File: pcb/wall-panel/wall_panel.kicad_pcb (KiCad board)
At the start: 6 copper layers, 75 x 79 mm, 121 parts, among them J1 USB_C_Receptacle_USB2.0_14P, J10 THD-20-R, J15 THD-20-R, J16 Micro_SD_Card_Det, J17 USB_C_Receptacle_USB2.0_14P, J18 THD-20-R, J2 USB_C_Receptacle_USB2.0_14P, J4 Conn_01x02_Socket, J5 F31L-1A7H1-11030, J6 690-019-298-412, SW1 power reset, SW2 cpu reset, U1 FSUSB42MUX, U10 RT9742GGJ5, U11 MT3608, U2 USB2514B-I/M2, U3 TPD4EUSB30, U4 AP22653W6, U5 DS3231M, U6 RT9742SNGV, U7 LP5907MFX-2.8, U9 74LVC1G07SE-7, Y1 ABM8G-24.000MHZ-18-D2Y-T

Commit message: wall panel v0.3
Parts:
- removed kibuzzard-68AB3EB0: G***, kibuzzard-68AB3EB0
- removed kibuzzard-6960BEF1: G***, kibuzzard-6960BEF1
- added kibuzzard-6981E919: G***, kibuzzard-6981E919, B.Cu at (69.8, 131.0)
- added kibuzzard-6984C46F: G***, kibuzzard-6984C46F, B.Cu at (111.5, 129.2)
- J5: value F31L-1A7H1-11030 -> SFV30R-4STBE1HLF; footprint F31L-1A7H1-11030:F31L1A7H111030 -> SFV30R-4STBE1HLF:SFV30R4STBE1HLF
- JP3, JP4: moved to F.Cu
- moved JP3 6.41 mm to (94.8, 69.0), turned to 0 degrees
- moved JP1 5.97 mm to (80.6, 88.1)
- moved JP4 1.57 mm to (89.0, 69.0), turned to 180 degrees
- moved J5 1.13 mm to (91.7, 75.2)
- moved R8 0.50 mm to (84.7, 116.2)
- moved C23 0.49 mm to (97.5, 82.1)
- moved C24 0.49 mm to (87.0, 82.1)
- moved C25 0.49 mm to (98.5, 82.1)
- moved C26 0.49 mm to (88.0, 82.1)
- moved C27 0.49 mm to (96.5, 82.1)
- moved C28 0.49 mm to (86.0, 82.1)
- moved C29 0.49 mm to (95.5, 82.1)
- moved C30 0.49 mm to (85.0, 82.1)
- moved R14 0.49 mm to (91.2, 82.1)
- moved R15 0.49 mm to (92.2, 82.1)
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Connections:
- net /CM4_HighSpeed/BACKLIGHT_POWER_OUT renamed /CM4_HighSpeed/BACKLIGHT_POWER
- C17 pad 1: Net-(J4-Pin_2) -> Net-(J4-Pin_1)
- J4 pad 1: GND -> Net-(J4-Pin_1)
- J4 pad 2: Net-(J4-Pin_2) -> GND
- JP3 pad 1: /CM4_GPIO ( Ethernet, GPIO, SDCARD)/GPIO4 -> /CM4_GPIO ( Ethernet, GPIO, SDCARD)/ID_SD
- JP3 pad 3: /CM4_GPIO ( Ethernet, GPIO, SDCARD)/ID_SD -> /CM4_GPIO ( Ethernet, GPIO, SDCARD)/GPIO4
- JP4 pad 1: /CM4_GPIO ( Ethernet, GPIO, SDCARD)/GPIO5 -> /CM4_GPIO ( Ethernet, GPIO, SDCARD)/ID_SC
- JP4 pad 3: /CM4_GPIO ( Ethernet, GPIO, SDCARD)/ID_SC -> /CM4_GPIO ( Ethernet, GPIO, SDCARD)/GPIO5
- U5 pad 14: Net-(J4-Pin_2) -> Net-(J4-Pin_1)
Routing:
- net Net-(J4-Pin_1): track 0.00 -> 15.1 mm
- net Net-(J4-Pin_2): track 14.0 -> 0.00 mm
- net /CM4_HighSpeed/TOUCH_SCL: track 21.0 -> 29.1 mm, vias 1 -> 2
- net /CM4_GPIO ( Ethernet, GPIO, SDCARD)/GPIO3: track 182.7 -> 174.8 mm
- net /CM4_GPIO ( Ethernet, GPIO, SDCARD)/GPIO2: track 187.7 -> 179.8 mm
- net /CM4_GPIO ( Ethernet, GPIO, SDCARD)/GPIO4: track 113.7 -> 121.1 mm, vias 2 -> 3
- net /CM4_GPIO ( Ethernet, GPIO, SDCARD)/GPIO_VREF: track 13.6 -> 7.61 mm
- net /CM4_GPIO ( Ethernet, GPIO, SDCARD)/+1.8v: track 14.7 -> 8.75 mm
- net /CM4_GPIO ( Ethernet, GPIO, SDCARD)/ID_SD: track 90.0 -> 95.5 mm, vias 2 -> 3
- net /CM4_HighSpeed/DSI1_C_N: track 35.0 -> 31.1 mm
- net /CM4_HighSpeed/TOUCH_SDA: track 19.6 -> 22.9 mm, vias 1 -> 2
- net /CM4_GPIO ( Ethernet, GPIO, SDCARD)/ID_SC: track 101.2 -> 98.9 mm, vias 2 -> 3
- net /CM4_GPIO ( Ethernet, GPIO, SDCARD)/GPIO5: track 90.6 -> 88.5 mm, vias 2 -> 3
- net /CM4_HighSpeed/BACKLIGHT_POWER: track 62.9 -> 64.7 mm, vias 4 -> 5
- net Net-(J1-CC2): track 8.33 -> 9.73 mm
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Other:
- outline, holes or cut-outs redrawn
- board text added: "Touch I2C config"

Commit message: small fixes of v0.3.1
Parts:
- added S3: SKSLLBE010, SKSLLBE010:SKSLLBE010, F.Cu at (127.9, 123.2)
- added S4: SKSLLBE010, SKSLLBE010:SKSLLBE010, F.Cu at (55.8, 117.2)
- added S5: SKSLLBE010, SKSLLBE010:SKSLLBE010, F.Cu at (55.8, 123.2)
- moved D1 6.27 mm to (121.5, 124.2)
- moved D2 6.27 mm to (121.5, 122.5)
- moved R16 6.27 mm to (118.7, 124.2)
- moved kibuzzard-68AC3314 1.50 mm to (60.5, 116.2)
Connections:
- net Net-(Module1A-PI_nLED_Activity) renamed /CM4_GPIO ( Ethernet, GPIO, SDCARD)/nActivity_LED
- J5 pad 8: unconnected-(J5-Pad8) -> /CM4_GPIO ( Ethernet, GPIO, SDCARD)/GPIO12
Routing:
- net /CM4_GPIO ( Ethernet, GPIO, SDCARD)/GPIO26: track 65.1 -> 89.6 mm
- net /CM4_GPIO ( Ethernet, GPIO, SDCARD)/GPIO12: track 70.4 -> 89.0 mm, vias 2 -> 3
- net /CM4_GPIO ( Ethernet, GPIO, SDCARD)/nActivity_LED: track 91.4 -> 84.8 mm
- net +3.3V: track 123.5 -> 117.1 mm
- net Net-(D2-K): track 72.1 -> 65.9 mm
- net /CM4_GPIO ( Ethernet, GPIO, SDCARD)/nPWR_LED: track 19.5 -> 14.1 mm
- net /CM4_HighSpeed/USBOTG_ID: track 45.0 -> 40.2 mm
- net /CM4_GPIO ( Ethernet, GPIO, SDCARD)/GPIO21: track 137.6 -> 140.2 mm, vias 3 -> 4
- net GND: vias 113 -> 115
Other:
- outline, holes or cut-outs redrawn

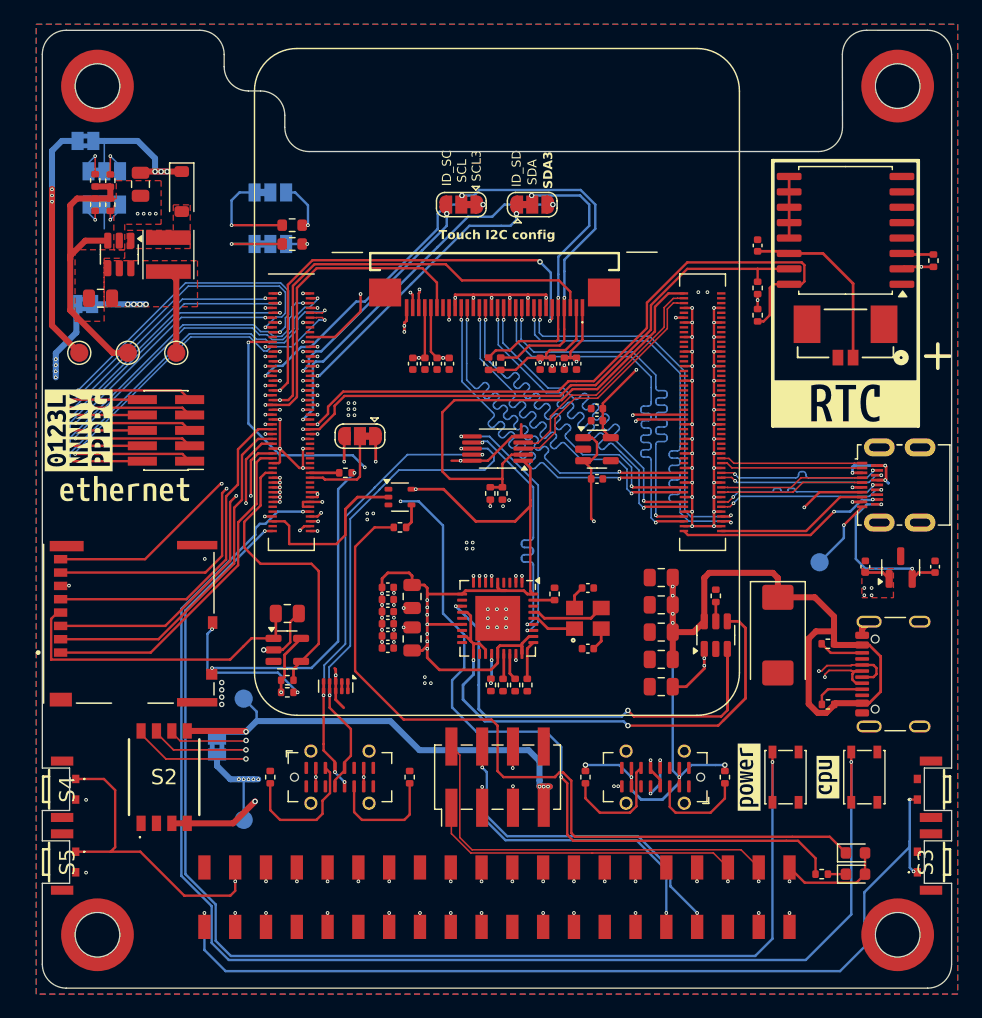
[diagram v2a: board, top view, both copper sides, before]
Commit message: pogo pins wall panel
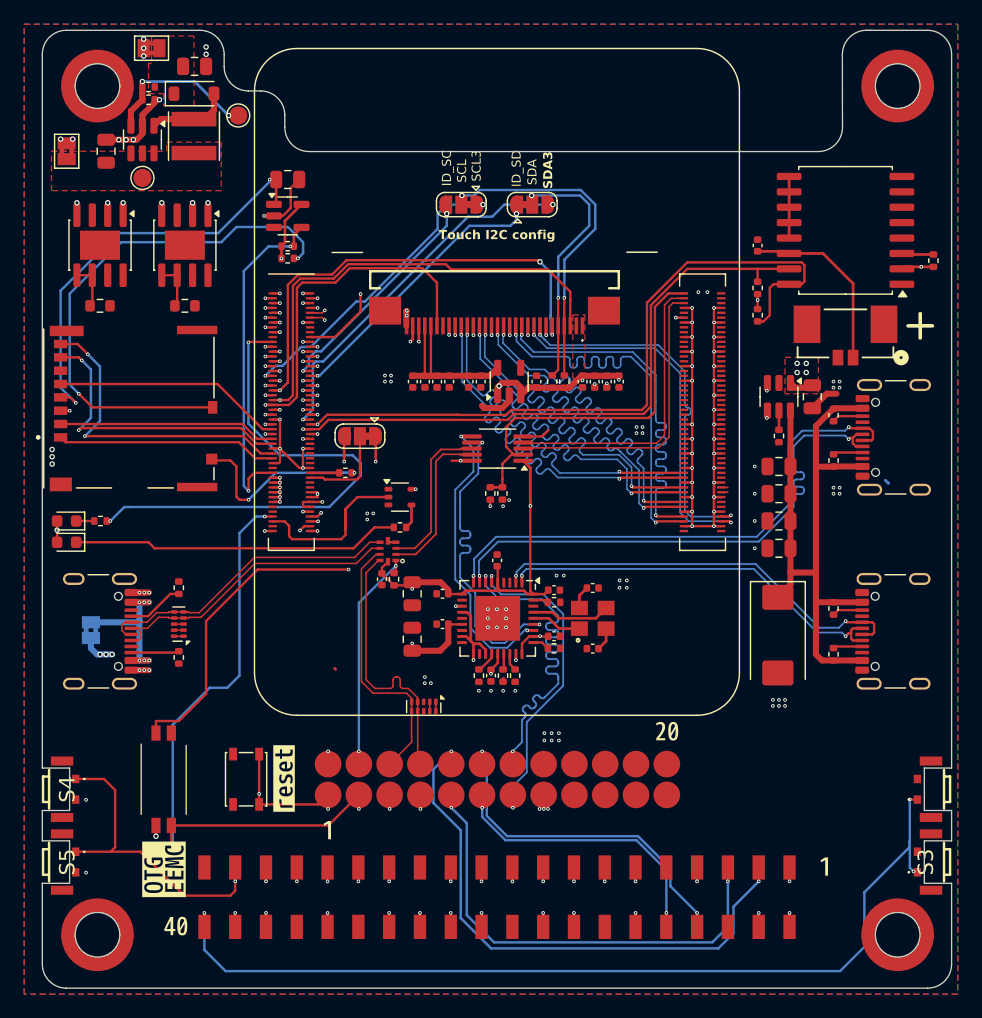
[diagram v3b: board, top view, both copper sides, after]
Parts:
- removed C18, C19: 100n, Capacitor_SMD:C_0402_1005Metric
- removed J15: THD-20-R, Connector_PinHeader_1.27mm:PinHeader_2x05_P1.27mm_Vertical_SMD
- removed J18: THD-20-R, Connector_PinHeader_2.54mm:PinHeader_2x04_P2.54mm_Vertical_SMD
- removed J6: 690-019-298-412, Connector_Video:HDMI_Micro-D_Molex_46765-1x01
- removed JP10, JP9: 0/110ohm, Jumper:SolderJumper-3_P1.3mm_Bridged12_Pad1.0x1.5mm
- removed JP7, JP8: 12.8/15V, Jumper:SolderJumper-3_P1.3mm_Bridged12_Pad1.0x1.5mm
- removed R18: 10K, Resistor_SMD:R_0402_1005Metric
- removed R27, R28: 110, Resistor_SMD:R_0603_1608Metric
- removed S2: 218-4LPSTRF, 218-4LPSTRF:2184LPSTRF
- removed SW2: cpu reset, Button_Switch_SMD:SW_SPST_PTS810
- removed TP1, TP2, TP6: TestPoint, TestPoint:TestPoint_Pad_D1.5mm
- removed TP4: boost out, TestPoint:TestPoint_Pad_D1.5mm
- removed U6: RT9742SNGV, Package_TO_SOT_SMD:SOT-23
- removed kibuzzard-68AB3D2F: G***, kibuzzard-68AB3D2F
- removed kibuzzard-68F10531: G***, kibuzzard-68F10531
- removed kibuzzard-68F10A66: G***, kibuzzard-68F10A66
- removed kibuzzard-68F655E1: G***, kibuzzard-68F655E1
- removed kibuzzard-68F655EA: G***, kibuzzard-68F655EA
- removed kibuzzard-6984C46F: G***, kibuzzard-6984C46F
- added C34: 100n, Capacitor_SMD:C_0402_1005Metric, F.Cu at (82.4, 99.9)
- added IC1: TS3USB221RSER, TS3USB221RSER:RSE_R-PUQFN-N10_, F.Cu at (82.9, 97.6)
- added J11: pogo_2-1_3, pogo:pogo_1x3, F.Cu at (80.5, 117.7)
- added J12: pogo_2-4_6, pogo:pogo_1x3, F.Cu at (88.1, 117.7)
- added J13: pogo_2-7_9, pogo:pogo_1x3, F.Cu at (95.7, 117.7)
- added J14: pogo_2-10_12, pogo:pogo_1x3, F.Cu at (103.4, 117.7)
- added J3: pogo_1-1_3, pogo:pogo_1x3, F.Cu at (80.5, 115.2)
- added J7: pogo_1-4_6, pogo:pogo_1x3, F.Cu at (88.1, 115.2)
- added J8: pogo_1-7_9, pogo:pogo_1x3, F.Cu at (95.7, 115.2)
- added J9: pogo_1-10_12, pogo:pogo_1x3, F.Cu at (103.4, 115.2)
- added R31: 2.4R, Resistor_SMD:R_0603_1608Metric, F.Cu at (66.2, 77.3)
- added R32: 2.4R, Resistor_SMD:R_0603_1608Metric, F.Cu at (59.1, 77.3)
- added S6: 218-2LPSTRF, 218-2LPSTRF:2182LPSTRF, F.Cu at (64.4, 116.4)
- added U12: OC7140, OC7140:ESOP-8, F.Cu at (59.1, 72.3)
- added U13: TPD4EUSB30, Package_SON:USON-10_2.5x1.0mm_P0.5mm, F.Cu at (85.8, 110.4)
- added U8: OC7140, OC7140:ESOP-8, F.Cu at (66.2, 72.3)
- added kibuzzard-6A266BA6: G***, kibuzzard-6A266BA6, F.Cu at (64.4, 123.8)
- added kibuzzard-6A266BBE: G***, kibuzzard-6A266BBE, F.Cu at (74.3, 116.3)
- added kibuzzard-6A2675C8: G***, kibuzzard-6A2675C8, F.Cu at (77.9, 120.6)
- added kibuzzard-6A2675C8: G***, kibuzzard-6A2675C8, F.Cu at (118.9, 123.6)
- added kibuzzard-6A2675F6: G***, kibuzzard-6A2675F6, F.Cu at (65.4, 128.5)
- added kibuzzard-6A267621: G***, kibuzzard-6A267621, F.Cu at (105.9, 112.4)
- added kibuzzard-6A294290: G***, kibuzzard-6A294290, B.Cu at (111.5, 129.2)
- J1, J2: footprint Connector_USB:USB_C_Receptacle_G-Switch_GT-USB-7051x -> Connector_USB:USB_C_Receptacle_GCT_USB4105-xx-A_16P_TopMnt_Horizontal
- JP5, JP6: moved to F.Cu
- R17: value 200K -> 100K
- moved kibuzzard-68AC3314 76.1 mm to (120.2, 69.0), turned to 180 degrees
- moved D1 71.3 mm to (56.4, 95.1), turned to 180 degrees
- moved D2 69.9 mm to (56.4, 96.8), turned to 180 degrees
- moved R16 66.2 mm to (59.2, 95.1), turned to 0 degrees
- moved SW1 44.5 mm to (71.2, 116.4), turned to -90 degrees
- moved R17 40.4 mm to (83.4, 99.9)
- moved R12 36.2 mm to (119.7, 86.4)
- moved C31 35.8 mm to (74.6, 66.9)
- moved R20 35.8 mm to (74.6, 73.4)
- moved R22 35.8 mm to (74.6, 72.4)
- moved U10 35.8 mm to (74.6, 69.9)
- moved J2 34.9 mm to (125.7, 88.2), turned to 90 degrees
- moved R10 27.6 mm to (119.7, 90.1), turned to -90 degrees
- moved C11 27.0 mm to (117.9, 84.8), turned to -90 degrees
- moved J1 24.1 mm to (58.1, 104.2), turned to -90 degrees
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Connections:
- J1 pad A4: /USB2-HUB/OTG_5V_IN -> /VBUS
- J1 pad A6: /USB2-HUB/USBD_P -> /USB2-HUB/USBD_OTG_P
- J1 pad A7: /USB2-HUB/USBD_N -> /USB2-HUB/USBD_OTG_N
- J1 pad A9: /USB2-HUB/OTG_5V_IN -> /VBUS
- J1 pad B4: /USB2-HUB/OTG_5V_IN -> /VBUS
- J1 pad B6: /USB2-HUB/USBD_P -> /USB2-HUB/USBD_OTG_P
- J1 pad B7: /USB2-HUB/USBD_N -> /USB2-HUB/USBD_OTG_N
- J1 pad B9: /USB2-HUB/OTG_5V_IN -> /VBUS
- J17 pad A6: /USB2-HUB/HD4_P -> /USB2-HUB/HD1_P
- J17 pad A7: /USB2-HUB/HD4_N -> /USB2-HUB/HD1_N
- J17 pad B6: /USB2-HUB/HD4_P -> /USB2-HUB/HD1_P
- J17 pad B7: /USB2-HUB/HD4_N -> /USB2-HUB/HD1_N
- J17 pad S1: GND -> unconnected-(J17-SHIELD-PadS1)
- J2 pad A6: /USB2-HUB/HD1_P -> /USB2-HUB/HD4_P
- J2 pad A7: /USB2-HUB/HD1_N -> /USB2-HUB/HD4_N
- J2 pad B6: /USB2-HUB/HD1_P -> /USB2-HUB/HD4_P
- J2 pad B7: /USB2-HUB/HD1_N -> /USB2-HUB/HD4_N
- J5 pad 2: Net-(J5-LEDK1_2) -> /CM4_HighSpeed/LEDK1
- J5 pad 3: Net-(J5-LEDK2_3) -> /CM4_HighSpeed/LEDK2
- J5 pad 7: unconnected-(J5-Pad7) -> /CM4_HighSpeed/DISPLAY_T
- J5 pad 8: /CM4_GPIO ( Ethernet, GPIO, SDCARD)/GPIO12 -> /CM4_HighSpeed/DISPLAY_PWM
- R17 pad 1: Net-(U11-FB) -> +3.3V
- R17 pad 2: Net-(JP7-B) -> /CM4_GPIO ( Ethernet, GPIO, SDCARD)/USB_OTG_SWITCH
- R29 pad 1: Net-(JP8-A) -> GND
- R30 pad 2: Net-(JP7-A) -> Net-(D3-K)
- U3 pad 4: /USB2-HUB/USBD_N -> /USB2-HUB/USBD_OTG_P
- U3 pad 5: /USB2-HUB/USBD_P -> /USB2-HUB/USBD_OTG_N
- U3 pad 6: /USB2-HUB/USBD_P -> /USB2-HUB/USBD_OTG_N
- U3 pad 7: /USB2-HUB/USBD_N -> /USB2-HUB/USBD_OTG_P
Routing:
- net /CM4_GPIO ( Ethernet, GPIO, SDCARD)/RUN_PG: track 114.5 -> 0.58 mm, vias 2 -> 1
- net /CM4_GPIO ( Ethernet, GPIO, SDCARD)/GLOBAL_EN: track 104.0 -> 34.2 mm, vias 2 -> 3
- net +3.3V: track 117.1 -> 70.7 mm, vias 23 -> 19
- net /CM4_HighSpeed/DISPLAY_PWM: track 0.00 -> 46.0 mm, vias 0 -> 3
- net /CM4_GPIO ( Ethernet, GPIO, SDCARD)/nActivity_LED: track 84.8 -> 42.5 mm, vias 4 -> 2
- net /CM4_HighSpeed/LEDK2: track 0.00 -> 41.1 mm, vias 0 -> 2
- net Net-(D2-K): track 65.9 -> 27.1 mm
- net /CM4_GPIO ( Ethernet, GPIO, SDCARD)/TRD0_P: track 37.2 -> 1.31 mm, vias 2 -> 1
- net /CM4_GPIO ( Ethernet, GPIO, SDCARD)/TRD1_P: track 36.5 -> 0.72 mm, vias 2 -> 1
- net /CM4_GPIO ( Ethernet, GPIO, SDCARD)/ETH_LEDG: track 35.1 -> 0.60 mm, vias 2 -> 1
- net /CM4_GPIO ( Ethernet, GPIO, SDCARD)/TRD0_N: track 34.9 -> 1.31 mm, vias 2 -> 1
- net /USB2-HUB/VBUS_OUT: track 85.3 -> 53.0 mm, vias 8 -> 0
- net /CM4_GPIO ( Ethernet, GPIO, SDCARD)/TRD1_N: track 32.7 -> 0.58 mm, vias 2 -> 1
- net /CM4_HighSpeed/LEDK1: track 0.00 -> 32.0 mm, vias 0 -> 2
- net /CM4_GPIO ( Ethernet, GPIO, SDCARD)/ETH_LEDY: track 32.4 -> 0.60 mm, vias 2 -> 1
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- added copper zone on F.Cu, net +3.3V
- added copper zone on In3.Cu, net +3.3V
- added copper zone on In4.Cu, net +5V
- added copper zone on In1.Cu, net GND
- added copper zone on In6.Cu, net GND
- added copper zone on F.Cu, net Net-(D3-K)
- removed copper zone on In1.Cu, net +2.8v
- removed copper zone on In1.Cu, net +3.3V
- removed copper zone on In1.Cu, net +5V
- removed copper zone on In2.Cu, net GND
- removed copper zone on In3.Cu, net GND
- removed copper zone on In4.Cu, net GND
- removed copper zone on F.Cu, net Net-(D3-A)
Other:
- copper layers 6 -> 8
- board text removed: "110"
- board text removed: "12.8V"
- board text removed: "15V"
- board text removed: "BL in"
- board text removed: "BL out"
- board text removed: "display R backlight"
